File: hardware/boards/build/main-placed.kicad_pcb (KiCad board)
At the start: 4 copper layers, 103 x 84 mm, 146 parts

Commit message: Multi algo
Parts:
- removed the REF** at (58.9, 78.5)
- removed the REF** at (76.5, 23.0)
- removed the REF** at (23.9, 9.05)
- removed the REF** at (51.9, 57.0) (x2)
- removed the REF** at (48.9, 5.05)
- removed the REF** at (96.0, 14.9)
- removed the REF** at (80.9, 73.5)
- removed the REF** at (49.0, 74.2)
- removed the REF** at (25.4, 75.0)
- removed the REF** at (76.5, 66.5)
- removed the REF** at (40.6, 56.9)
- removed the REF** at (70.6, 27.3)
- removed the REF** at (36.0, 66.8)
- removed the REF** at (65.4, 78.5)
- removed the REF** at (8.07, 21.2)
- removed the REF** at (70.5, 62.2)
- removed the REF** at (43.9, 72.0)
- added REF**: SOD-123, B5819W:SOD-123, F.Cu at (96.6, 32.7)
- added REF**: TSSOP-14, OPA4172ID:TSSOP-14, F.Cu at (72.3, 49.7)
- added REF**: SOT-23, BAT54S:SOT-23, F.Cu at (71.2, 57.2)
- added REF**: TSSOP-14, OPA4172ID:TSSOP-14, B.Cu at (68.7, 33.0)
- added REF**: SOT-23, BAT54S:SOT-23, B.Cu at (40.8, 60.3)
- added REF**: SOT-23, BAT54S:SOT-23, B.Cu at (56.2, 62.1)
- added REF**: SOT-23, BAT54S:SOT-23, B.Cu at (41.9, 23.9)
- added REF**: SOT-23, BAT54S:SOT-23, B.Cu at (56.3, 58.0)
- added REF**: SOT-23, 2N3904:SOT-23, B.Cu at (78.2, 39.9)
- added REF**: TSSOP-16, DAC8568SPMR:TSSOP-16, B.Cu at (68.9, 54.9)
- added REF**: SOD-123, B5819W:SOD-123, B.Cu at (54.5, 23.9)
- added REF**: SOT-23, BAT54S:SOT-23, B.Cu at (64.2, 60.3)
- added REF**: TSSOP-14, OPA4172ID:TSSOP-14, B.Cu at (68.9, 43.3)
- added REF**: SOT-23, 2N3904:SOT-23, F.Cu at (79.8, 36.4)
- added REF**: TSSOP-16, DAC8568SPMR:TSSOP-16, F.Cu at (49.1, 24.2)
- added REF**: TSSOP-14, OPA4172ID:TSSOP-14, F.Cu at (51.7, 59.3)
- added REF**: TSSOP-14, OPA4172ID:TSSOP-14, F.Cu at (69.0, 34.1)
- added REF**: SOD-123, B5819W:SOD-123, F.Cu at (33.2, 42.5)
- C1, C10, C11, C23, C25, C26, C28, C35, C39, C40, C41, C44, C6, R17, R20, R24, R3, R32, R34, R35, R37, R38, R4, R40, R42, R48, R49, R52, R7, R70: moved to B.Cu
- C12, C13, C18, C27, C31, C34, C43, R12, R16, R25, R27, R30, R36, R39, R44, R5, R50, R58, R6, R61, R64, R67, R68, R72, R8, REF**: moved to F.Cu
- moved C15 64.8 mm to (69.8, 28.4)
- moved R32 63.7 mm to (68.4, 59.5), turned to 180 degrees
- moved C4 62.0 mm to (62.1, 26.8)
- moved C2 59.3 mm to (46.7, 57.3)
- moved R68 59.2 mm to (74.8, 32.2), turned to 0 degrees
- moved REF** 58.8 mm to (64.4, 62.0), turned to 0 degrees
- moved R47 58.8 mm to (63.1, 24.1)
- moved C42 58.6 mm to (57.6, 62.2)
- moved C40 58.5 mm to (52.2, 59.6), turned to 180 degrees
- moved R63 57.7 mm to (60.0, 61.4)
- moved C17 57.6 mm to (42.8, 57.1)
- moved C29 56.2 mm to (70.6, 26.9)
- moved R57 55.6 mm to (58.3, 24.5)
- moved C45 55.2 mm to (41.1, 57.4)
- moved C24 54.1 mm to (43.2, 26.8)
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
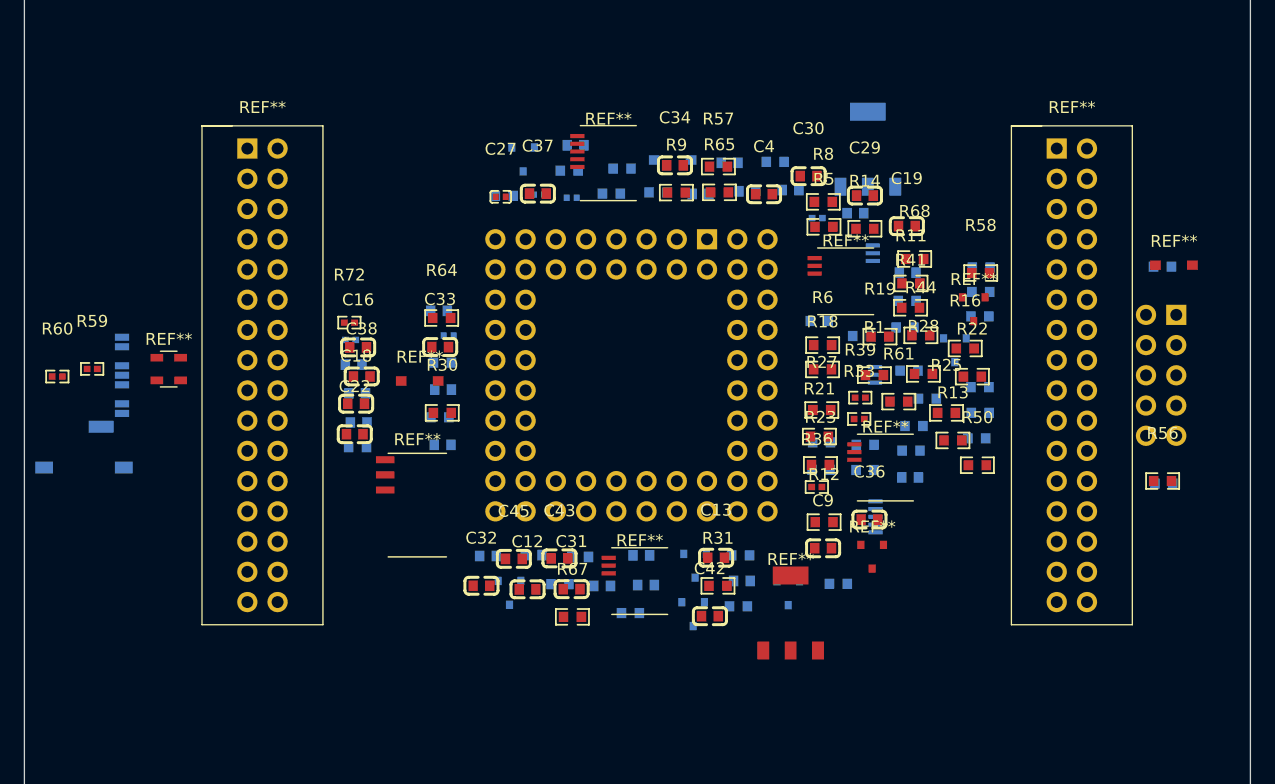
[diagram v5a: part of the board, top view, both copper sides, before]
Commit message: Multi algo parts placement and functioning gerber export
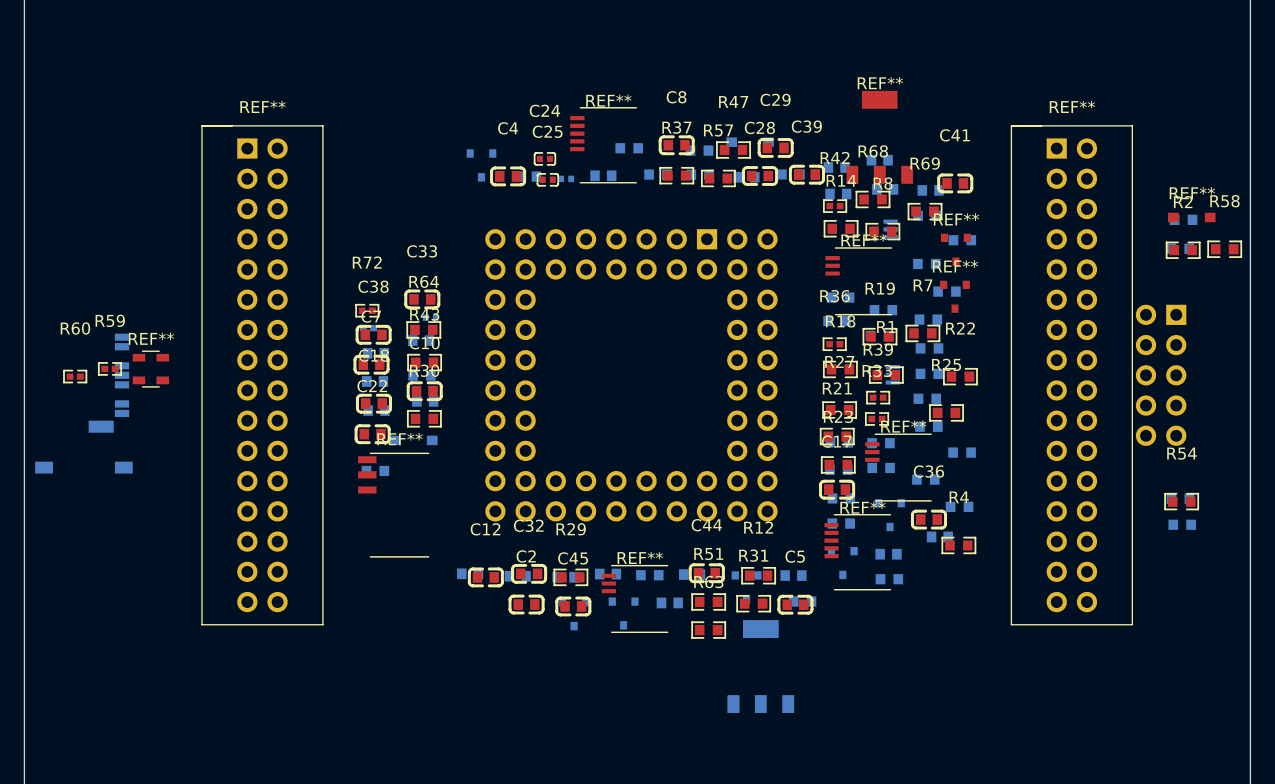
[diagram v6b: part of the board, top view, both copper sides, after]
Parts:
- C10, C17, C2, C24, C25, C28, C39, C41, C44, C5, C7, C8, R2, R29, R37, R4, R42, R43, R47, R51, R54, R63, R69, R7, REF** (x3): moved to F.Cu
- C13, C16, C19, C27, C30, C31, C34, C37, C42, C43, C9, R11, R13, R16, R28, R41, R44, R5, R50, R56, R6, R61, R65, R67, R9, REF** (x3): moved to B.Cu
- moved REF** 28.1 mm to (68.8, 57.8)
- moved C17 26.1 mm to (68.3, 51.6), turned to 0 degrees
- moved R52 24.4 mm to (97.3, 54.6)
- moved C4 21.6 mm to (40.6, 25.3)
- moved R58 20.6 mm to (100.8, 31.4)
- moved R3 17.5 mm to (97.4, 28.9)
- moved R2 17.4 mm to (97.4, 31.5), turned to 0 degrees
- moved R11 15.7 mm to (72.0, 49.8), turned to 180 degrees
- moved R70 14.6 mm to (78.8, 30.7)
- moved R55 13.1 mm to (75.8, 28.6)
- moved R66 12.7 mm to (72.7, 59.1)
- moved R51 12.6 mm to (57.5, 61.0), turned to 0 degrees
- moved R13 12.5 mm to (77.5, 35.0), turned to 180 degrees
- moved R36 12.1 mm to (68.1, 39.4)
- moved R46 11.2 mm to (50.8, 22.9)
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
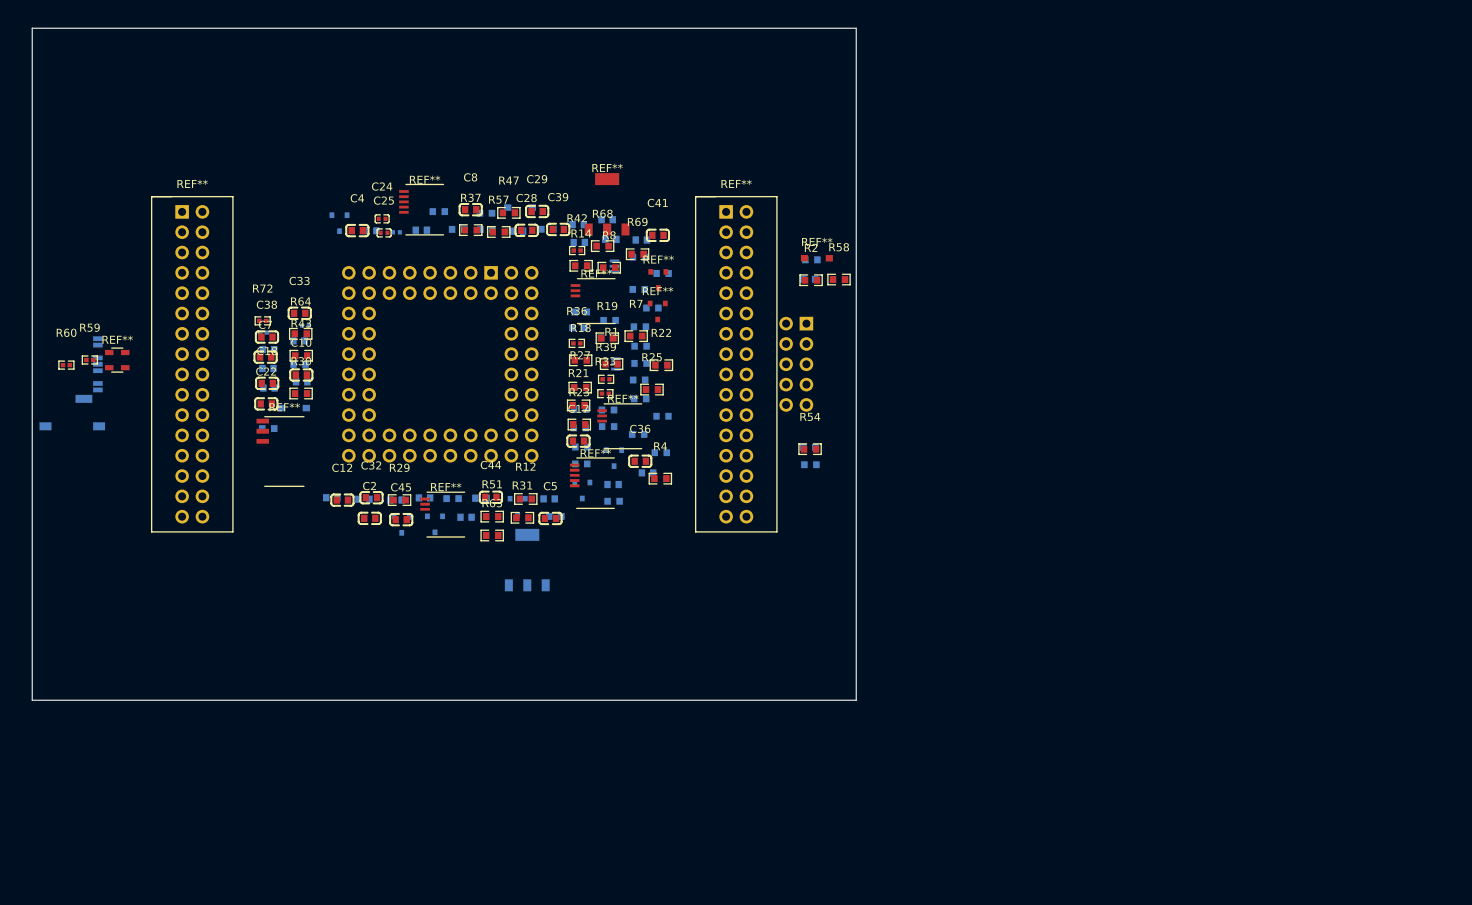
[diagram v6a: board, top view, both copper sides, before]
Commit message: Single sided SMD assebly
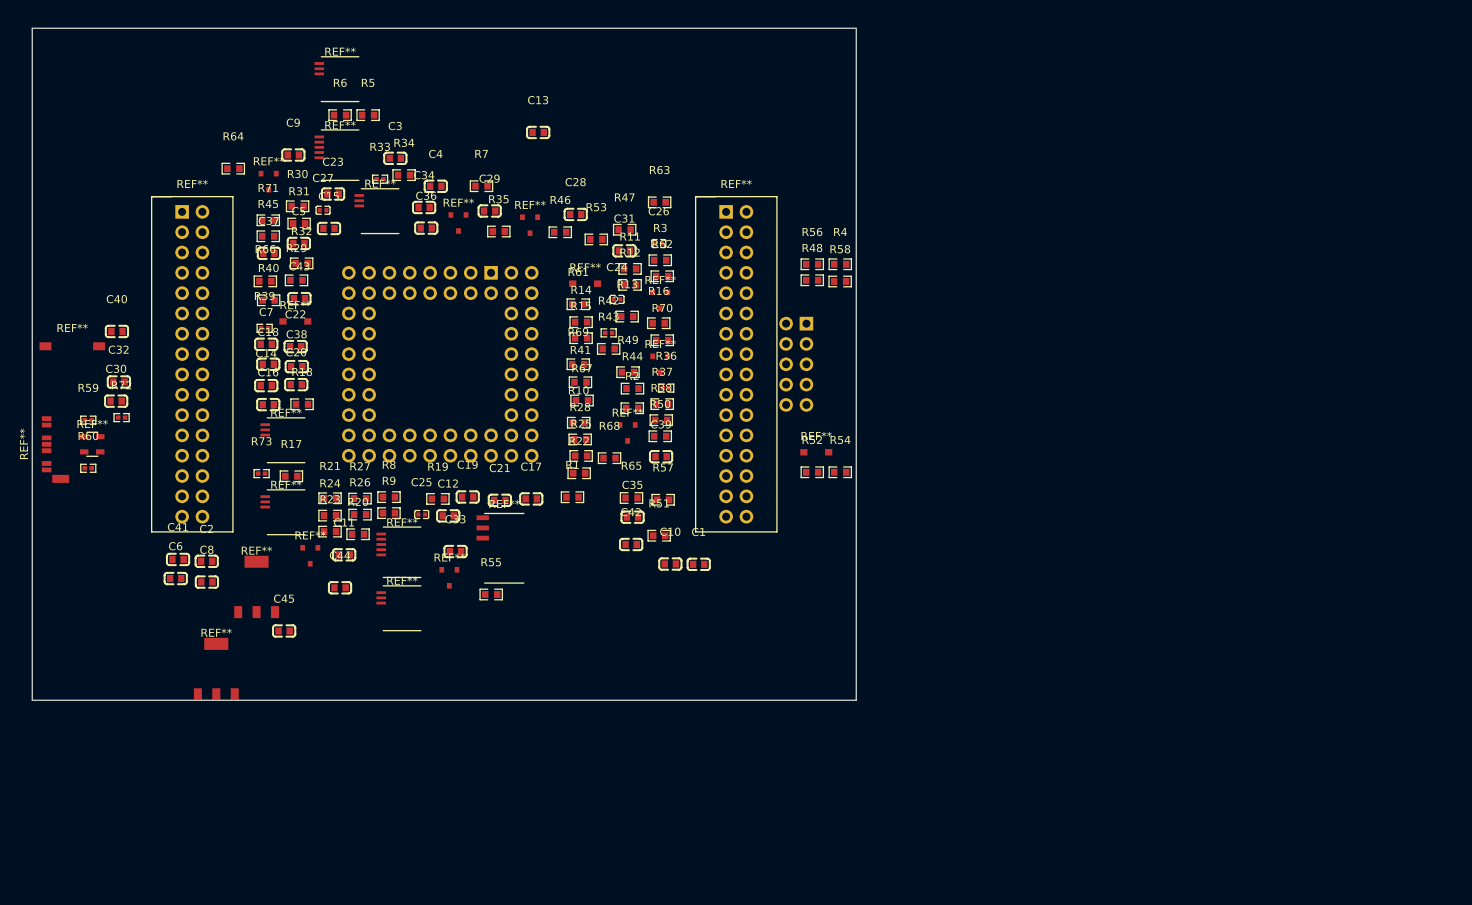
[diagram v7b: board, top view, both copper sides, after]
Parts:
- C1, C11, C13, C14, C15, C16, C19, C20, C21, C23, C26, C27, C3, C30, C31, C34, C35, C37, C40, C42, C43, C6, C9, R10, R11, R13, R15, R16, R17, R20, R24, R26, R28, R3, R32, R34, R35, R38, R40, R41, R44, R45, R46, R48, R49, R5, R50, R52, R53, R55, R56, R6, R61, R62, R65, R66, R67, R70, R71, R73, R9, REF** (x13): moved to F.Cu
- moved C41 72.4 mm to (18.2, 66.4)
- moved REF** 64.9 mm to (28.0, 69.8)
- moved C30 61.2 mm to (10.5, 46.6), turned to 0 degrees
- moved C9 57.4 mm to (32.6, 15.8), turned to 0 degrees
- moved C8 57.0 mm to (21.8, 69.2)
- moved C11 53.2 mm to (39.0, 65.8), turned to 0 degrees
- moved C23 52.5 mm to (37.6, 20.7), turned to 0 degrees
- moved REF** 52.0 mm to (38.5, 15.9)
- moved C10 51.8 mm to (79.8, 67.0)
- moved R66 51.5 mm to (29.1, 31.6), turned to 0 degrees
- moved C40 49.4 mm to (10.6, 37.9), turned to 0 degrees
- moved R63 46.6 mm to (78.4, 21.8)
- moved C5 46.6 mm to (33.3, 26.9)
- moved R31 46.2 mm to (33.4, 24.4)
- moved R55 46.0 mm to (57.4, 70.8), turned to 0 degrees
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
